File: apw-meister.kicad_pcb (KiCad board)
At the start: 6 copper layers, 13.2 x 30 mm, 36 parts, among them J1 USB_C_Receptacle_USB2.0, J2 Hashboard0, SW2 GT-TC029B-H025-L1N, SW3 GT-TC029B-H025-L1N, U1 SK6812, U2 W25Q16JVUXIQ, U3 RP2040, U4 AP2112K-3.3TRG1, Y1 12MHz

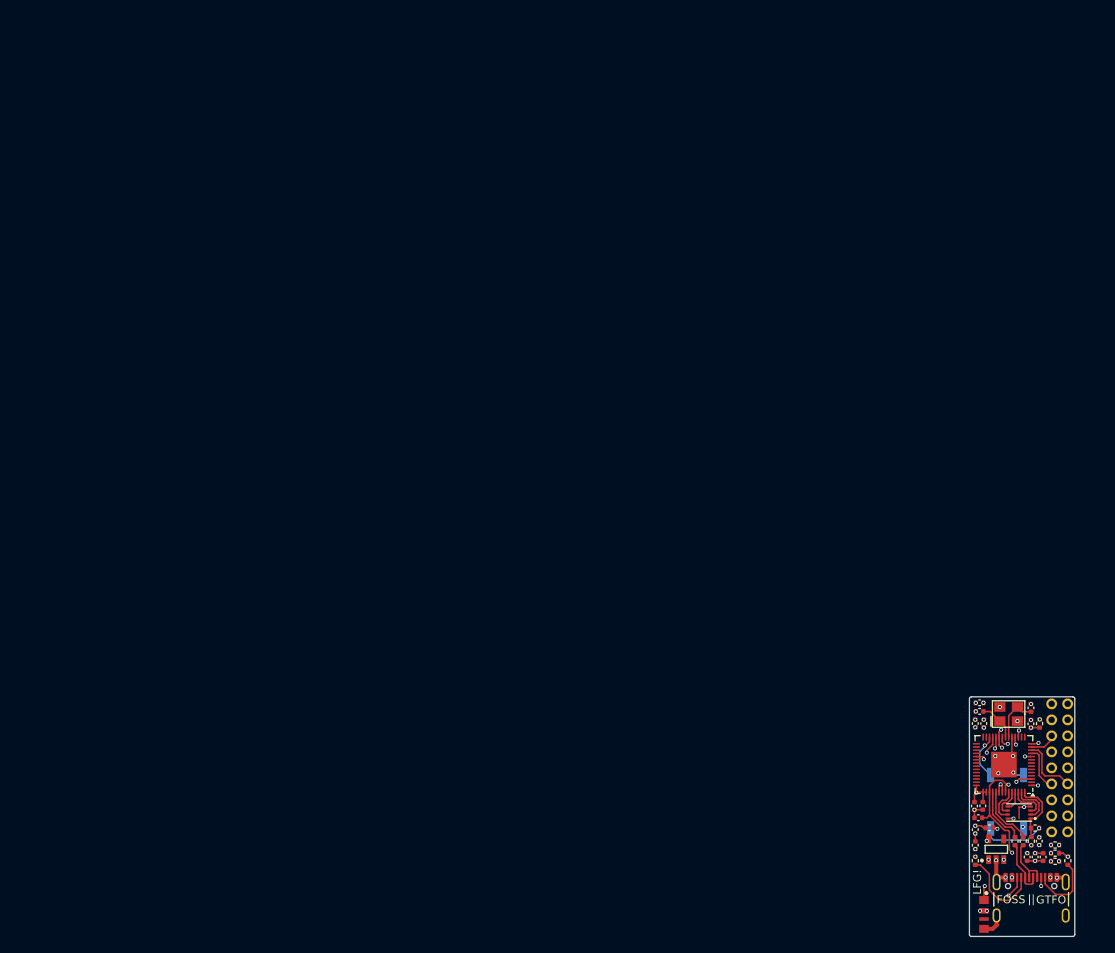
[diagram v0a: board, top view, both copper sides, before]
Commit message: Checkpoint RP2354A schematic, models, and initial PCB routing
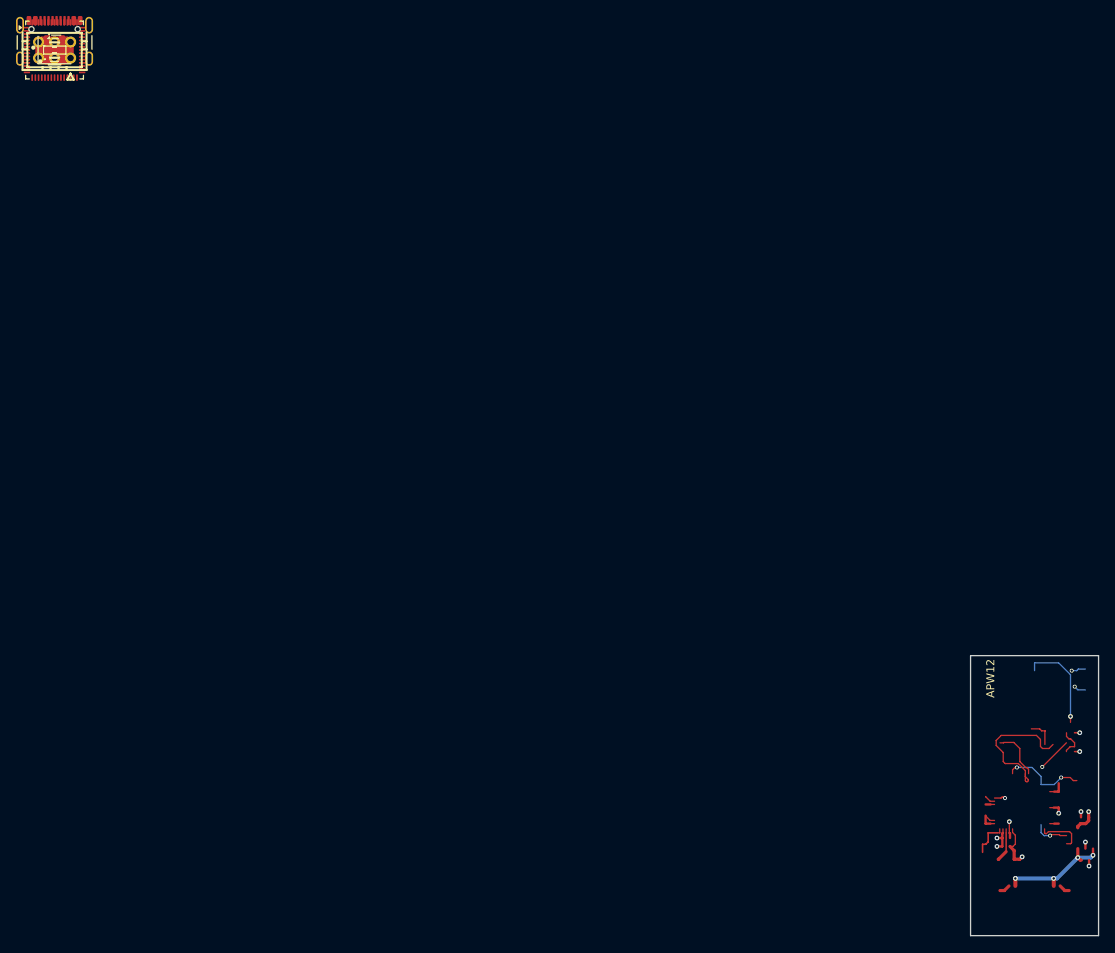
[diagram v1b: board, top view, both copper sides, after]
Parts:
- removed C5: 0.1uF, Capacitor_SMD:C_0402_1005Metric
- removed G***: LOGO, aditBoard:logo
- removed R1: 10k, Resistor_SMD:R_0402_1005Metric
- removed R25, R27, R29: 4.7K, Resistor_SMD:R_0402_1005Metric
- removed U2: W25Q16JVUXIQ, aditBoard:USON8_L2.0-W3.0-P0.50-BL-EP
- added C19, C20, C21, C22: 100nF, aditBoard:C_0402_1005Metric, F.Cu at (0.00, 0.00)
- added C23, C24: 4.7uF, aditBoard:C_0402_1005Metric, F.Cu at (0.00, 0.00)
- added L1: 3.3uH, aditBoard:L_Abracon_AOTA-B201610S3R3-101-T, F.Cu at (0.00, 0.00)
- added Q1: DMG1012T-7, aditBoard:SOT-523, F.Cu at (0.00, 0.00)
- added R10, R11: 4.7k, aditBoard:R_0402_1005Metric, F.Cu at (0.00, 0.00)
- added R12, R8: 1k, aditBoard:R_0402_1005Metric, F.Cu at (0.00, 0.00)
- added R13: 10k, aditBoard:R_0402_1005Metric, F.Cu at (0.00, 0.00)
- added R14: 33, aditBoard:R_0402_1005Metric, F.Cu at (0.00, 0.00)
- added R9: 330, aditBoard:R_0402_1005Metric, F.Cu at (0.00, 0.00)
- added TP1: APW12_PIN1, TestPoint:TestPoint_Pad_D1.0mm, B.Cu at (0.00, 0.00)
- added TP2: APW12_PIN4, TestPoint:TestPoint_Pad_D1.0mm, B.Cu at (0.00, 0.00)
- added U5: TPD6E05U06RVZR, aditBoard:Texas_R-PUSON-N14, F.Cu at (0.00, 0.00)
- added U6: TPD4E05U06DQAR, aditBoard:USON-10_2.5x1.0mm_P0.5mm, F.Cu at (0.00, 0.00)
- C10, C11, C12, C13, C14, C15, C16, C17, C18, C6, C7: footprint Capacitor_SMD:C_0402_1005Metric -> aditBoard:C_0402_1005Metric
- C2, C4: value 30pF -> 15pF; footprint Capacitor_SMD:C_0402_1005Metric -> aditBoard:C_0402_1005Metric
- C8, C9: value 1uF -> 4.7uF; footprint Capacitor_SMD:C_0402_1005Metric -> aditBoard:C_0402_1005Metric
- J1: value USB_C_Receptacle_USB2.0 -> USB4105-GF-A-120
- J2: value Hashboard0 -> APW12 PSU Comm; footprint aditBoard:PinHeader_2x09_P2.00mm_Horizontal -> aditBoard:CONN-TH_6P-P2.00_PHD-2X3A
- R2, R3: value 33 -> 27; footprint Resistor_SMD:R_0402_1005Metric -> aditBoard:R_0402_1005Metric
- R4, R5, R6, R7: footprint Resistor_SMD:R_0402_1005Metric -> aditBoard:R_0402_1005Metric
- SW2, SW3: value GT-TC029B-H025-L1N -> B3U-1000P; footprint aditBoard:SW_CS1213AGF260_CRS -> aditBoard:SW_SPST_B3U-1000P
- U1: value SK6812 -> SK6812SIDE-A-RVS
- U3: value RP2040 -> RP2354A; footprint Package_DFN_QFN:QFN-56-1EP_7x7mm_P0.4mm_EP3.2x3.2mm -> aditBoard:QFN-60-1EP_7x7mm_P0.4mm_EP3.4x3.4mm
- Y1: footprint aditBoard:OSC-SMD_4P-L3.2-W2.5-BL -> aditBoard:Crystal_SMD_3225-4Pin_3.2x2.5mm
- moved J1 162.4 mm to (0.00, 0.00)
- moved R5 162.2 mm to (0.00, 0.00), turned to 0 degrees
- moved C16 159.5 mm to (0.00, 0.00), turned to 0 degrees
- moved U1 158.7 mm to (0.00, 0.00), turned to 0 degrees
- moved C6 158.0 mm to (0.00, 0.00), turned to 0 degrees
- moved C15 157.9 mm to (0.00, 0.00), turned to 0 degrees
- moved R6 156.5 mm to (0.00, 0.00)
- moved R2 156.3 mm to (0.00, 0.00), turned to 0 degrees
- moved R3 155.5 mm to (0.00, 0.00), turned to 0 degrees
- moved U4 154.4 mm to (0.00, 0.00)
- moved SW2 153.8 mm to (0.00, 0.00)
- moved R4 153.3 mm to (0.00, 0.00), turned to 0 degrees
- moved C17 152.1 mm to (0.00, 0.00), turned to 0 degrees
- moved C18 152.0 mm to (0.00, 0.00)
- moved C9 150.8 mm to (0.00, 0.00), turned to 0 degrees
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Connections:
- net /5V renamed +5V
- net Net-(J1-CC1) renamed /CC1
- net Net-(J1-CC2) renamed /CC2
- net Net-(U3-RUN) renamed /RUN
- C10 pad 1: /GND -> GND
- C11 pad 1: /GND -> GND
- C12 pad 1: /GND -> GND
- C13 pad 1: /GND -> GND
- C14 pad 1: /GND -> GND
- C15 pad 1: /GND -> GND
- C16 pad 1: /GND -> GND
- C17 pad 2: /GND -> GND
- C18 pad 2: /GND -> GND
- C2 pad 1: /GND -> GND
- C2 pad 2: /XOUT -> Net-(C2-Pad2)
- C4 pad 1: /GND -> GND
- C6 pad 1: /GND -> GND
- C7 pad 1: /GND -> GND
- C8 pad 1: /GND -> /1V1
- C8 pad 2: /1V1 -> GND
- C9 pad 2: /GND -> GND
- J1 pad A1B12: /GND -> GND
- J1 pad B1A12: /GND -> GND
- J1 pad S1: /GND -> GND
- J2 pad 1: /GND -> /APW12_PIN1
- J2 pad 2: /GND -> GND
- J2 pad 3: /SDA -> /PSU_SDA
- J2 pad 4: /SCL -> /APW12_PIN4
- J2 pad 5: /PLUG -> /PSU_EN
- J2 pad 6: /A2 -> /PSU_SCL
- R2 pad 2: Net-(U3-USB_DP) -> /USB_DP_MCU
- R3 pad 2: Net-(U3-USB_DM) -> /USB_DN_MCU
- R4 pad 1: /GND -> GND
- R5 pad 1: /GND -> GND
- SW2 pad 2: /GND -> GND
- SW3 pad 2: /GND -> GND
- U1 pad 4: /GND -> GND
- U3 pad 10: /3V3 -> unconnected-(U3-GPIO7-Pad10)
- U3 pad 11: /TXD -> /3V3
- U3 pad 12: /RXD -> unconnected-(U3-GPIO8-Pad12)
- U3 pad 13: /PLUG -> unconnected-(U3-GPIO9-Pad13)
- U3 pad 14: /RST -> unconnected-(U3-GPIO10-Pad14)
- U3 pad 17: /SDA -> unconnected-(U3-GPIO13-Pad17)
- U3 pad 18: /SCL -> /PSU_SDA
- U3 pad 19: /GND -> /PSU_SCL
- U3 pad 20: /XIN -> /3V3
- U3 pad 21: /XOUT -> /XIN
- U3 pad 22: /3V3 -> /XOUT
- U3 pad 3: Net-(U1-DIN) -> /LED_DATA
- U3 pad 30: unconnected-(U3-GPIO19-Pad30) -> /3V3
- U3 pad 33: /3V3 -> unconnected-(U3-GPIO21-Pad33)
- U3 pad 37: unconnected-(U3-GPIO25-Pad37) -> /MCU_PSU_ON
- U3 pad 38: unconnected-(U3-GPIO26_ADC0-Pad38) -> /3V3
- U3 pad 39: unconnected-(U3-GPIO27_ADC1-Pad39) -> /1V1
- U3 pad 42: /3V3 -> unconnected-(U3-GPIO28/ADC2-Pad42)
- U3 pad 43: /3V3 -> unconnected-(U3-GPIO29/ADC3-Pad43)
- U3 pad 45: /1V1 -> /3V3
- U3 pad 46: Net-(U3-USB_DM) -> /VREG_AVDD
- U3 pad 47: Net-(U3-USB_DP) -> GND
- U3 pad 48: /3V3 -> /VREG_LX
- U3 pad 51: /QSPI_SD3 -> /USB_DN_MCU
- U3 pad 52: /QSPI_SCLK -> /USB_DP_MCU
- U3 pad 53: /QSPI_SD0 -> /3V3
- U3 pad 54: /QSPI_SD2 -> /3V3
- U3 pad 55: /QSPI_SD1 -> unconnected-(U3-QSPI_SD3-Pad55)
- U3 pad 56: /QSPI_SS -> unconnected-(U3-QSPI_SCLK-Pad56)
- U3 pad 57: /GND -> unconnected-(U3-QSPI_SD0-Pad57)
- U3 pad 6: unconnected-(U3-GPIO4-Pad6) -> /1V1
- U4 pad 2: /GND -> GND
- Y1 pad 1: /XOUT -> Net-(C2-Pad2)
- Y1 pad 2: /GND -> GND
- Y1 pad 4: /GND -> GND
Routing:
- net GND: track 0.00 -> 50.1 mm, vias 0 -> 7
- net /SWCLK: track 30.0 -> 0.00 mm, vias 2 -> 0
- net /SWD: track 27.8 -> 0.00 mm, vias 2 -> 0
- net /A2: track 21.9 -> 0.00 mm, vias 1 -> 0
- net /GND: track 21.7 -> 0.00 mm, vias 26 -> 0
- net Net-(U1-DIN): track 19.2 -> 0.00 mm, vias 2 -> 0
- net /A1: track 18.0 -> 0.00 mm, vias 1 -> 0
- net +5V: track 0.88 -> 15.3 mm, vias 7 -> 4
- net /1V1: track 29.4 -> 16.1 mm, vias 6 -> 2
- net /XOUT: track 4.84 -> 17.8 mm
- net /A0: track 12.5 -> 0.00 mm, vias 1 -> 0
- net /PSU_EN: track 0.00 -> 12.0 mm, vias 0 -> 1
- net /MCU_PSU_ON: track 0.00 -> 11.9 mm, vias 0 -> 2
- net /RST: track 11.0 -> 0.00 mm, vias 1 -> 0
- net /CC1: track 10.7 -> 0.00 mm
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- removed copper zone on In2.Cu, net +5V
- removed copper zone on In3.Cu, net /3V3
- removed copper zone on In1.Cu, net /GND
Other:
- board size 13.2 x 30 mm -> 16 x 35 mm
- board text added: "APW12"
- board text added: "BOOT"
- board text added: "RESET"
- board text added: "USB"
- board text added: "apw-meister"
- board text removed: "FOSS"
- board text removed: "GTFO"
- board text removed: "LFG!"
- board text removed: "v2"
- board text removed: "||"

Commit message: Migrate apw-meister hardware to CH32X035F8U6
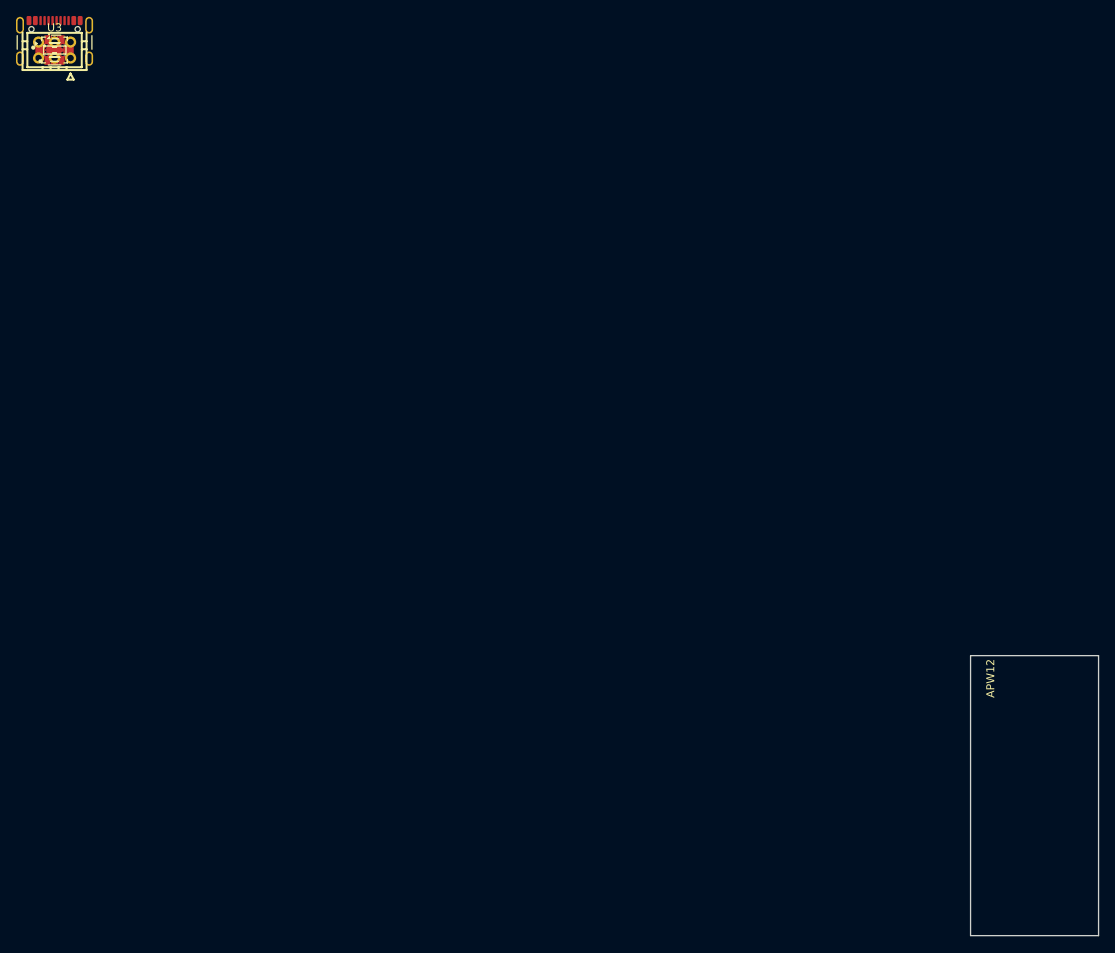
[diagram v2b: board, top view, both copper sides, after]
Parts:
- removed C11, C12, C13, C14, C15, C16, C6, C7: 0.1uF, aditBoard:C_0402_1005Metric
- removed C2, C4: 15pF, aditBoard:C_0402_1005Metric
- removed C20, C21, C22: 100nF, aditBoard:C_0402_1005Metric
- removed C23, C24, C8, C9: 4.7uF, aditBoard:C_0402_1005Metric
- removed L1: 3.3uH, aditBoard:L_Abracon_AOTA-B201610S3R3-101-T
- removed R14: 33, aditBoard:R_0402_1005Metric
- removed R8: 1k, aditBoard:R_0402_1005Metric
- removed Y1: 12MHz, aditBoard:Crystal_SMD_3225-4Pin_3.2x2.5mm
- added Q2, Q3: DMG1012T-7, aditBoard:SOT-523, F.Cu at (0.00, 0.00)
- R2, R3: value 27 -> 0
- R6: value 1k -> 4.7k
- TP1, TP2: footprint TestPoint:TestPoint_Pad_D1.0mm -> aditBoard:TestPoint_Pad_D1.0mm
- U3: value RP2354A -> CH32X035F8U6; footprint aditBoard:QFN-60-1EP_7x7mm_P0.4mm_EP3.4x3.4mm -> aditBoard:VQFN-20-1EP_3x3mm_P0.4mm_EP1.7x1.7mm
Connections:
- net Net-(Q1-G) renamed /PSU_GATE
- J1 pad A8: /SWCLK -> /SDI_CLK
- J1 pad B8: /SWD -> /SDI_DIO
- R10 pad 2: /PSU_SDA -> /MCU_PSU_SDA
- R11 pad 2: /PSU_SCL -> /MCU_PSU_SCL
- R6 pad 1: /QSPI_SS -> /3V3
- R7 pad 1: /RUN -> +5V
- R7 pad 2: /3V3 -> /REG_EN
- SW2 pad 2: GND -> /USB_DP_MCU
- SW3 pad 1: /RUN -> /REG_EN
- U3 pad 11: /3V3 -> unconnected-(U3-PB1-Pad11)
- U3 pad 14: unconnected-(U3-GPIO10-Pad14) -> /SDI_DIO
- U3 pad 16: unconnected-(U3-GPIO12-Pad16) -> /SDI_CLK
- U3 pad 17: unconnected-(U3-GPIO13-Pad17) -> /USB_DN_MCU
- U3 pad 18: /PSU_SDA -> /USB_DP_MCU
- U3 pad 19: /PSU_SCL -> unconnected-(U3-PC14/CC1-Pad19)
- U3 pad 2: unconnected-(U3-GPIO0-Pad2) -> /MCU_PSU_SDA
- U3 pad 20: /3V3 -> unconnected-(U3-PC15/CC2-Pad20)
- U3 pad 21: /XIN -> GND
- U3 pad 3: /LED_DATA -> /MCU_PSU_SCL
- U3 pad 6: /1V1 -> /MCU_PSU_ON
- U3 pad 9: unconnected-(U3-GPIO6-Pad9) -> /LED_DATA
- U4 pad 3: +5V -> /REG_EN
- U5 pad 8: /SWD -> /SDI_DIO
- U5 pad 9: /SWCLK -> /SDI_CLK
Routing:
- net GND: track 50.1 -> 0.00 mm, vias 7 -> 0
- net /3V3: track 25.1 -> 0.00 mm, vias 2 -> 0
- net /XOUT: track 17.8 -> 0.00 mm
- net /1V1: track 16.1 -> 0.00 mm, vias 2 -> 0
- net +5V: track 15.3 -> 0.00 mm, vias 4 -> 0
- net /PSU_EN: track 12.0 -> 0.00 mm, vias 1 -> 0
- net /MCU_PSU_ON: track 11.9 -> 0.00 mm, vias 2 -> 0
- net /RUN: track 10.6 -> 0.00 mm, vias 2 -> 0
- net /XIN: track 6.48 -> 0.00 mm
- net /QSPI_SS: track 5.94 -> 0.00 mm
- net /VREG_AVDD: track 4.91 -> 0.00 mm
- net /APW12_PIN1: track 4.52 -> 0.00 mm, vias 1 -> 0
- net Net-(R6-Pad2): track 4.45 -> 0.00 mm, vias 1 -> 0
- net /APW12_PIN4: track 4.44 -> 0.00 mm, vias 1 -> 0
- net /VREG_LX: track 4.24 -> 0.00 mm
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
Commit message: Compact and route CH32 PCB with rear buttons and logo
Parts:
- added G***: LOGO, apw-meister-logo, B.Cu at (0.00, 0.00)
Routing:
- net /USB_DP_MCU: track 0.00 -> 19.9 mm, vias 0 -> 2
- net /SDI_DIO: track 0.00 -> 19.6 mm, vias 0 -> 3
- net GND: track 0.00 -> 18.1 mm, vias 0 -> 16
- net /REG_EN: track 0.00 -> 17.6 mm, vias 0 -> 1
- net /PSU_SCL: track 0.00 -> 15.9 mm, vias 0 -> 2
- net /PSU_EN: track 0.00 -> 15.5 mm, vias 0 -> 1
- net /3V3: track 0.00 -> 12.1 mm, vias 0 -> 5
- net /USB_DP: track 0.00 -> 11.6 mm, vias 0 -> 2
- net /MCU_PSU_SDA: track 0.00 -> 10.4 mm, vias 0 -> 2
- net Net-(R6-Pad2): track 0.00 -> 10.3 mm, vias 0 -> 1
- net /CC2: track 0.00 -> 10.3 mm, vias 0 -> 2
- net /PSU_SDA: track 0.00 -> 9.78 mm
- net /USB_DN: track 0.00 -> 9.64 mm, vias 0 -> 2
- net /SDI_CLK: track 0.00 -> 8.84 mm, vias 0 -> 2
- net /CC1: track 0.00 -> 8.35 mm, vias 0 -> 3
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- added copper zone on In3.Cu, net +5V
- added copper zone on In2.Cu, net /3V3
- added copper zone on B.Cu, net GND
- added copper zone on F.Cu, net GND
- added copper zone on In1.Cu, net GND
- added copper zone on In4.Cu, net GND
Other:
- board size 16 x 35 mm -> 14 x 28 mm
- board text removed: "apw-meister"
